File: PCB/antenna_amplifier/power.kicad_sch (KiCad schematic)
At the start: 22 parts, among them J101 PWR_IN 9V, U101 ADM7150ARDZ-5.0, U102 ADM7150ARDZ-3.3

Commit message: Add two-bucket isolated PSU and the PC analysis software
PSU (PCB/acdc_converter/design.py, generated schematic, ERC clean):
Mains -> IRM-05-15 -> LM317 constant-current (0.2 A) / constant-voltage
(10.9 V) supercap charger -> two 4 x 10 F buckets swapped every ~30 s by
two Omron G6K-2 DPDT relays wired in opposite senses. Form-C contacts
break before make, so the receiver ground is never connected to the
charger side; the only coupling left is the open-contact capacitance
(~1 pF) instead of the AC-DC barrier (20-100 pF). The receiver side
adds a reservoir, an LT3045 (0.8 uV rms, EN/PGFB to IN, 22 uF C_SET for
low 1/f noise) and a common-mode choke. Charger ground is bonded to PE
and the enclosure; the only LED is on the mains-powered charger side.

Software (software/elara): streaming decimator, PLL-locked NLMS mains
canceller (>60 dB with drift, 45 Hz tone untouched), L/R Wiener noise
reference subtraction, front-end response correction, Lorentzian
Schumann fit, sferic detector, simulator and CLI; 27 pytest tests.

Generator: explicit wires, net labels on wires, touching and stacked
pins, labels-only symbols.

Co-Authored-By: Claude Opus 5.5 <noreply@anthropic.com>
Claude-Session: https://claude.ai/code/session_01RsM1DhHhY1tSr2aHjVygSC
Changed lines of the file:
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@@
 		(dnp no)
 		(property "Reference" "D102"
-			(at 57.95 61.23 270)
+			(at 57.95 61.23 90)
 			(effects
 				(font
@@
 		)
 		(property "Value" "SMAJ15A"
-			(at 57.95 63.83 270)
+			(at 57.95 63.83 90)
 			(effects
 				(font

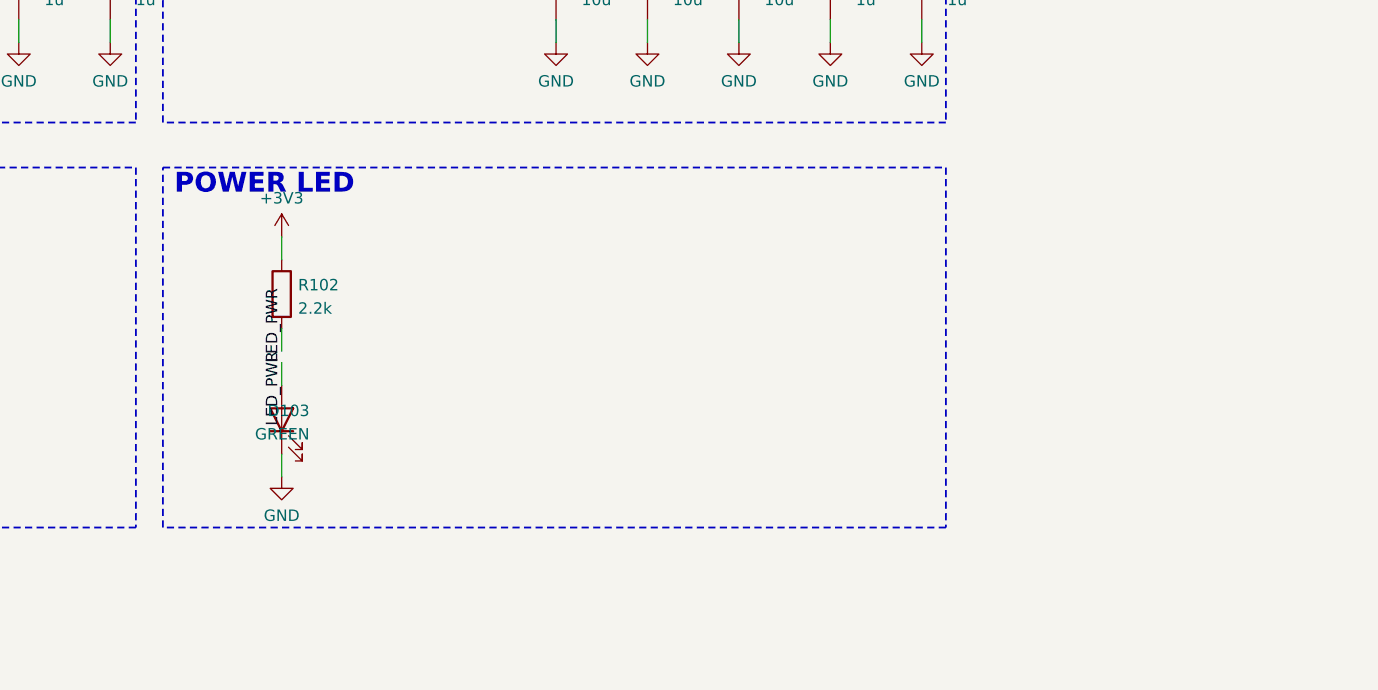
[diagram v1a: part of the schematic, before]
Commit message: Drop amplifier power LED, add turret and pulse-transformer footprints, start PCB generator
The amplifier board can run from a battery, so it has no power LED;
the overload LED only lights while the ADC clips. Adds PCB/elara.pretty
(PTFE input turret, DIP-6 digital-audio transformer outline -- pinout
to be verified against the Newava datasheet) and a work-in-progress
pcbnew-based layout generator.

Co-Authored-By: Claude Opus 5.5 <noreply@anthropic.com>
Claude-Session: https://claude.ai/code/session_01RsM1DhHhY1tSr2aHjVygSC
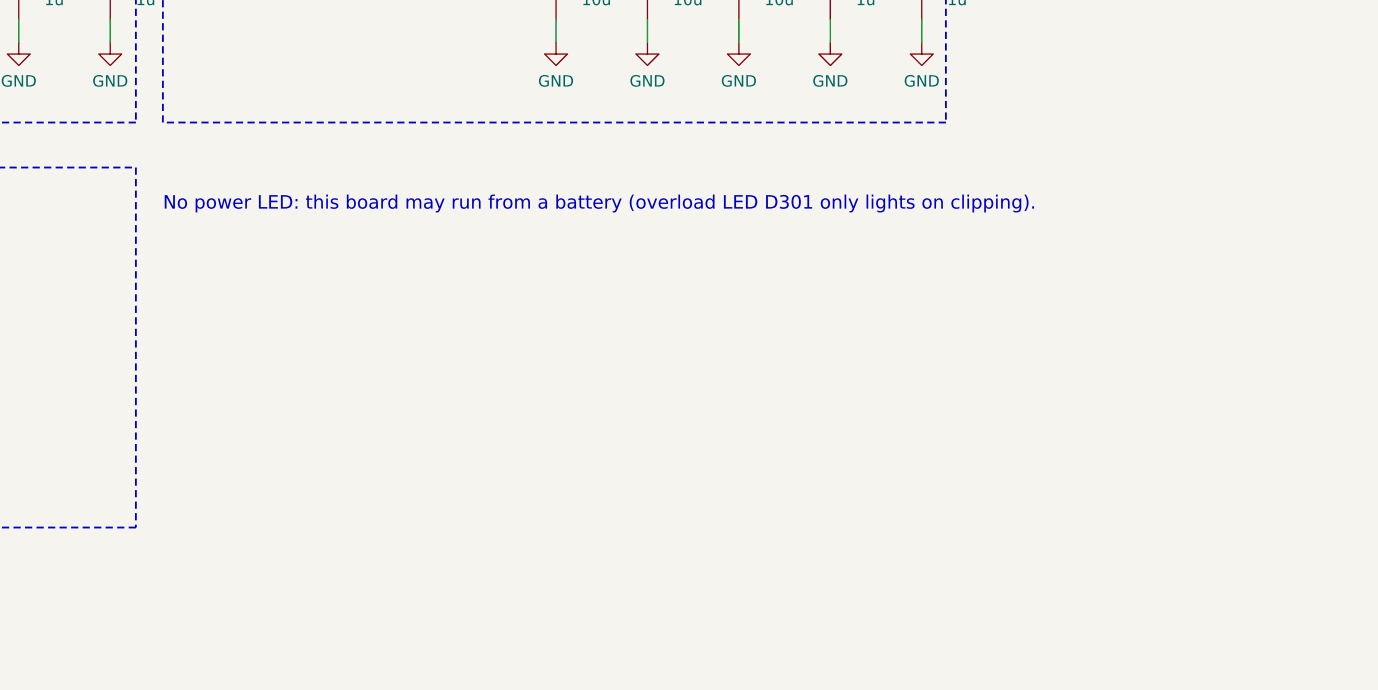
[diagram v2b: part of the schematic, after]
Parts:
- removed D103: GREEN, LED_SMD:LED_0805_2012Metric, symbol Device:LED
- removed R102: 2.2k, Resistor_SMD:R_0603_1608Metric, symbol Device:R
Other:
- note added: "No power LED: this board may run from a battery (overload LED D301 only lights on clipping)."
- note removed: "POWER LED"

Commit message: Route the two-bucket PSU board: fully connected, DRC clean but one thermal
Freerouting 1.9 in batch mode (2.1 never saved its session). Grounds
are routed on this board because the relays switch bucket current in
the unpoured area; mains nets 1.0 mm / 2.0 mm, current paths 0.6 mm;
hand-routed 1 mm PE rail on the left edge, GND_C-PE bond at the PE
hole; only the two mains-side holes are PE, the receiver-side holes
are unplated. Plain exposed-pad footprints (the thermal-via variants
need 0.2 mm drills). Newava S2208x redrawn as a 4-pin part (windings
1-2 / 3-4 per the DCR spec) with slotted pins 2/4 fitting either pitch.

Co-Authored-By: Claude Opus 5.5 <noreply@anthropic.com>
Claude-Session: https://claude.ai/code/session_01RsM1DhHhY1tSr2aHjVygSC
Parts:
- U101, U102: footprint Package_SO:SOIC-8-1EP_3.9x4.9mm_P1.27mm_EP2.29x3mm_ThermalVias -> Package_SO:SOIC-8-1EP_3.9x4.9mm_P1.27mm_EP2.29x3mm
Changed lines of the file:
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@@
 			)
 		)
-		(property "Footprint" "Package_SO:SOIC-8-1EP_3.9x4.9mm_P1.27mm_EP2.29x3mm_ThermalVias"
+		(property "Footprint" "Package_SO:SOIC-8-1EP_3.9x4.9mm_P1.27mm_EP2.29x3mm"
 			(at 123.19 45.72 0)
 			(effects
@@
 			)
 		)
-		(property "Footprint" "Package_SO:SOIC-8-1EP_3.9x4.9mm_P1.27mm_EP2.29x3mm_ThermalVias"
+		(property "Footprint" "Package_SO:SOIC-8-1EP_3.9x4.9mm_P1.27mm_EP2.29x3mm"
 			(at 213.36 45.72 0)
 			(effects

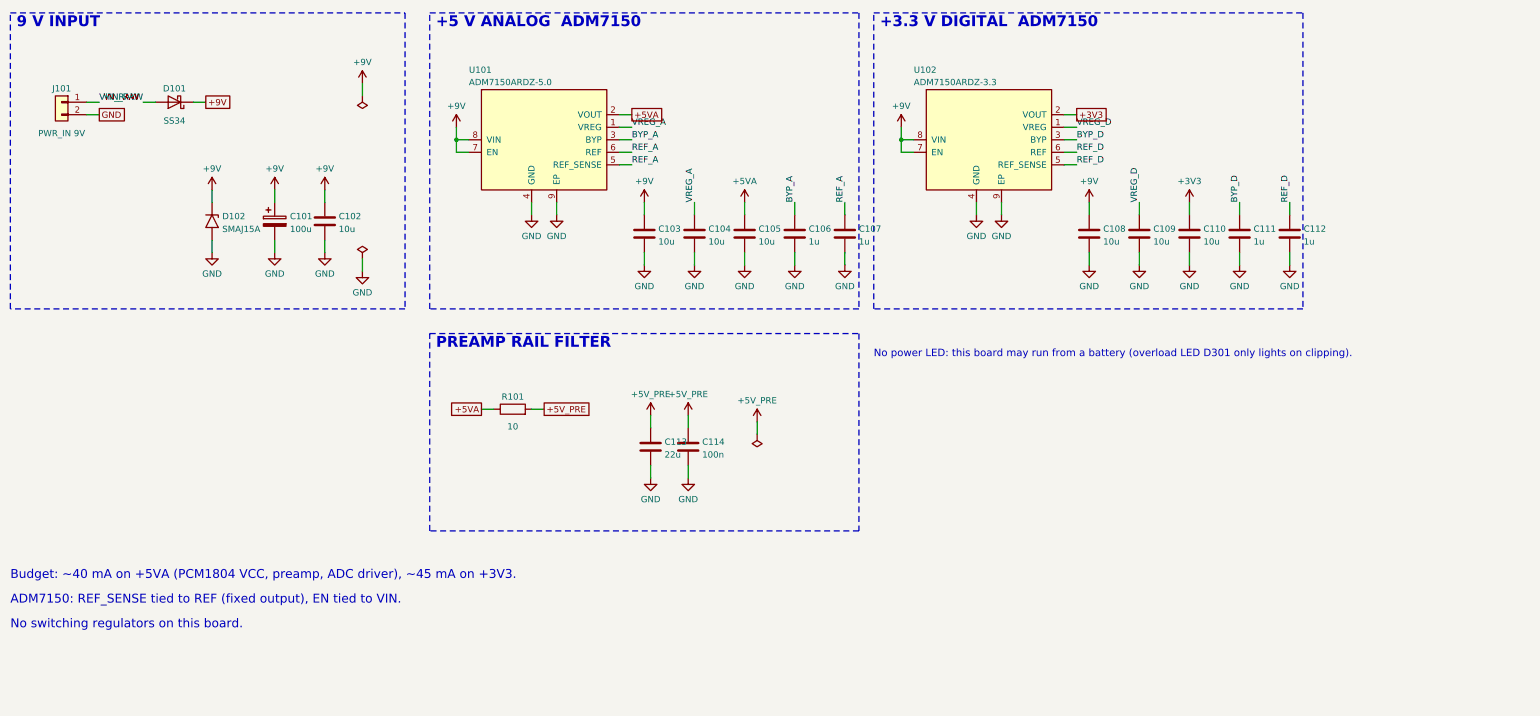
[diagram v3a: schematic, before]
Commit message: Pedantic schematic and silkscreen pass: zero overlaps, labels clear of tracks
Schematics
- tools/kicadgen/schcheck.py checks KiCad's own SVG rendering (exact stroke boxes)
  for text over text, lines through text, crowded twin labels and text outside the
  frame. Both schematics: 0 findings; ERC 0 on both.
- Generator: Sheet.join (one wire + one label instead of two facing labels),
  per-symbol field positions, per-pin stub lengths, shared power symbol for
  adjacent top/bottom rail pins, crowded rail runs get one label, longer PCM1804
  pins (no-connect cross clear of the pin number), PE value clear of its symbol.
- Fixed: doubled VIN_RAW/BIAS_DIV/LED_OVF/CV_ADJ/LED_C labels, +5VA vs VREG,
  +5V_PRE twins, CS8406 GND straps vs neighbours, BNC/LED/diode fields over their
  graphics, bucket-cell values vs tap labels, notes outside the frame, J2 -> J202.
- Root sheet: sub-sheets in signal-flow order with arrows and a design summary;
  dated title blocks.

Boards
- References prefer spots clear of tracks as well as parts (two candidate rings);
  compartment labels are re-placed after routing; the title block on the back is
  placed as one unit; no stitching via under any board text.
- DRC with schematic parity: amplifier 0 errors / 0 unconnected / 0 parity (only
  the intended bare-island mask warnings); PSU and plate 0 of anything.

Co-Authored-By: Claude Opus 5.5 <noreply@anthropic.com>
Claude-Session: https://claude.ai/code/session_01RsM1DhHhY1tSr2aHjVygSC
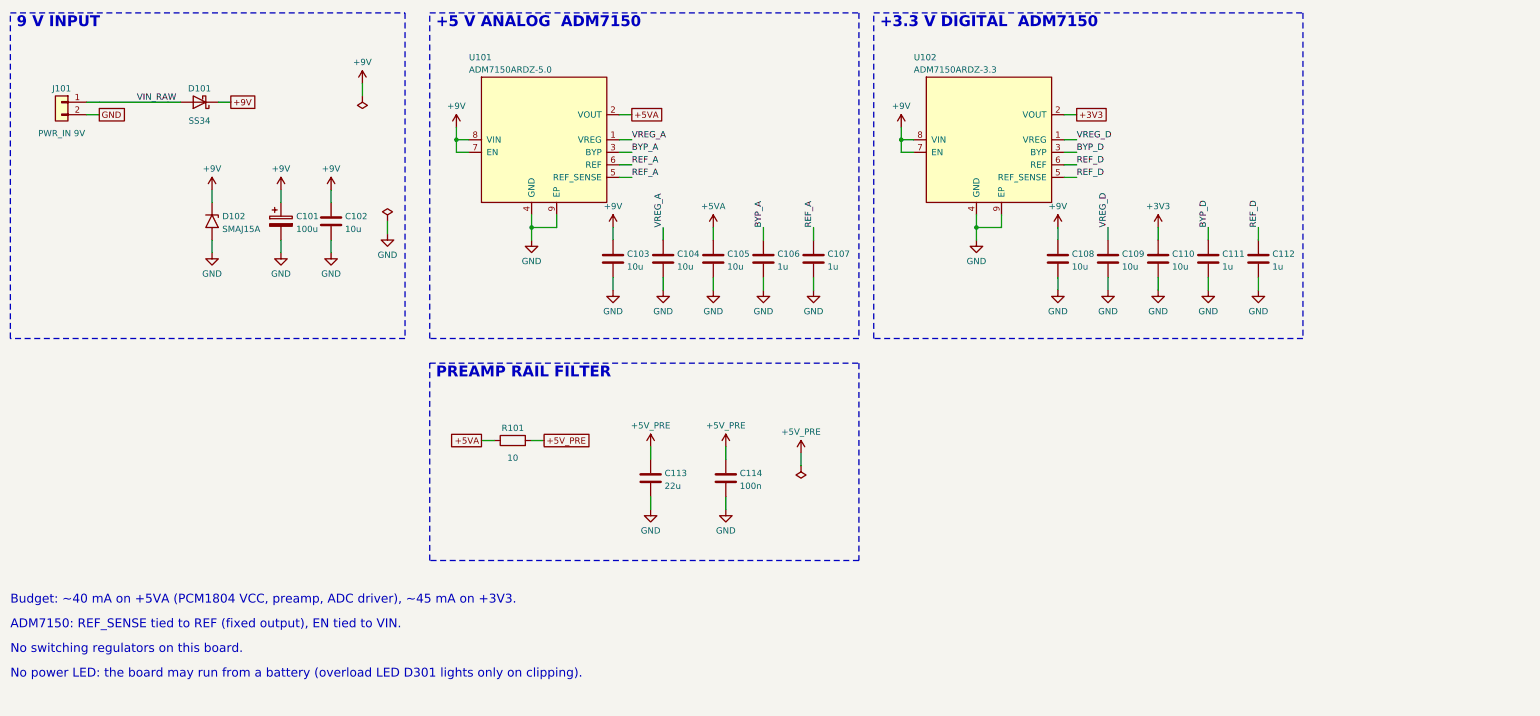
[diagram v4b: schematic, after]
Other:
- note added: "No power LED: the board may run from a battery (overload LED D301 lights only on clipping)."
- note removed: "No power LED: this board may run from a battery (overload LED D301 only lights on clipping)."
- moved on the sheet: C101, C102, C103, C104, C105, C106, C107, C108, C109, C110, C111, C112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

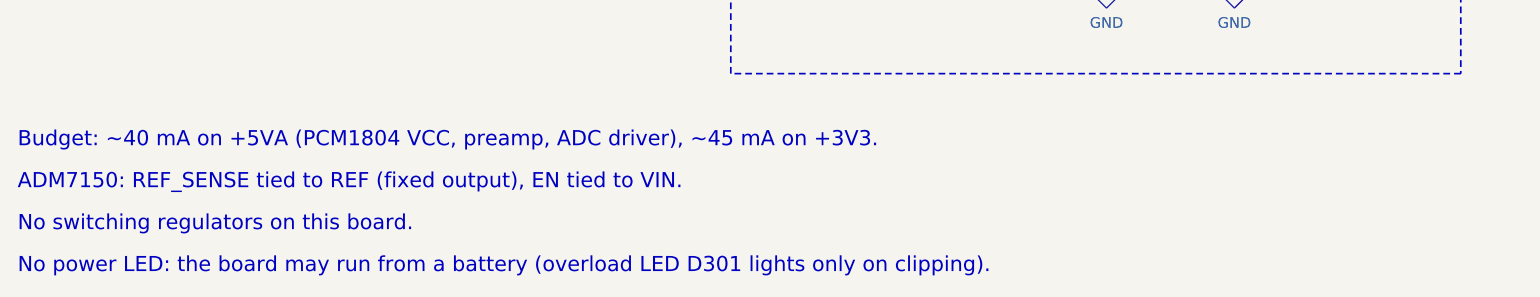
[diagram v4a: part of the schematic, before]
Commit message: Battery-friendly amplifier, RJ45 AES3 output, tidy placement, 1 mm PSU barrier
Amplifier schematic:
- No LEDs (battery use): the D301 overflow LED becomes test point TP301.
- PCM1804 FMT/S-M/OSR pins use the chip's internal 51 k pull-downs (6 resistors
  gone); BYPAS and the CS8406 mode pins get 47 k: about 3 mA less on +3V3.
- One output: AES3 on a shielded RJ45 (Amphenol RJHSE-5380, blue pair 4/5) for
  shielded twisted-pair cable, transformer isolated; the cable shield floats at
  the receiver (10 nF RF bond DNP, the DC bond is gone). The S/PDIF coax branch
  (BNC, second S22083, 5.6 mA standing current) is removed.

Layout:
- Amplifier re-placed in functional blocks on a 0.5 mm grid: PCM1804 and CS8406
  side by side so the I2S lines run straight, capacitor cells round the LDOs,
  DIP pull-downs in line with the switch pins, guard column in signal order with
  a re-routed hand guard-drive link. RJ45 notch 20 x 16 mm, BNC notch gone.
- PSU tidied (aligned columns, flyback diodes over their relays) and the charger
  / receiver copper kept >= 1.0 mm apart (was 0.30 mm): custom DRC rule, 1 mm
  router class for the relay contacts, hand-routed GND / GND_C at the relays.
- Reference labels follow each part's row; every label on silk except on the
  bare guard island. Fixed two placer bugs: each label counted as its own
  obstacle (SWIG proxies compared with 'is'), and unplaced labels blocked their
  neighbours. Texts are measured by their strokes, not KiCad's text cell.

Mechanics: RJ45 notch, plug envelope and a 1 mm isolation gap in fit_check.
BOM: 502 EUR as designed, 407 EUR recommended; 81 order lines.
Docs: STATUS, PLAN, ASSEMBLY, MOUNTING, README, mechanical and BOM notes;
MAINS_CABLE gains a certified DIY screened-cable option (H07RN-F + foil + braid)
and says why Ethernet cable must not carry mains.

All checks pass (tools/check_all.sh): ERC 0, DRC/parity 0 on all boards (only
the intended guard-island mask bridges), mains clearances, fit check, 27 tests.

Co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
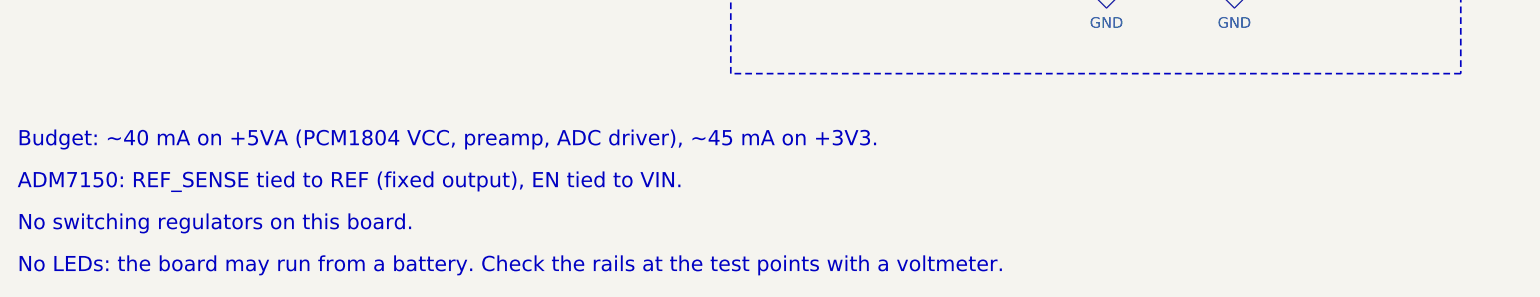
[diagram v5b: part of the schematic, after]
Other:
- note added: "No LEDs: the board may run from a battery. Check the rails at the test points with a voltmeter."
- note removed: "No power LED: the board may run from a battery (overload LED D301 lights only on clipping)."

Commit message: AES3 source resistors 22 ohm for a 111 ohm source; tidy schematics and assembly drawings
- R412/R413 2 x 39 -> 2 x 22 ohm (Vishay TNPW060322R0BEEA, anti-sulfur): the
  CS8406 drivers are 33.5 ohm each at VL = 3.3 V, so 2 x 39 gave a 145 ohm
  source, outside AES3's 110 ohm +-20 %. The schematic note had used the 5 V
  figure and mis-added it.
- AES3 sheet: transformer flipped (kicadgen gains mirror='x') and wired straight
  to R412/R413/C405 and the RJ45, no more touching AES_HOT/AES_COLD labels.
- Stale S/PDIF and 9 V wording out of the sheets and BOM: DC input block reads
  6.98-15 V, J101 'DC IN', PSU J2 'DC OUT', reset button and clock branch say
  AES3; the legacy +9V / +9V_OUT net names are explained on the sheets.
- PSU root sheet gets the same power-path / board summary as the amplifier.
- Assembly drawings: fab-layer copies of the references removed wherever the
  silk reference shows (KiCad 9 texts cannot be hidden), so each part is named
  once; J201/J202 (no silk on the guard island) get theirs beside the part.
- BOM totals +0.14 EUR (502.15 ex VAT reference build, 407.22 recommended).

Co-Authored-By: Claude Opus 5.5 <noreply@anthropic.com>
Claude-Session: https://claude.ai/code/session_01RsM1DhHhY1tSr2aHjVygSC
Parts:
- J101: value PWR_IN 9V -> DC IN
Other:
- note added: "DC INPUT 6.98-15 V"
- note added: "No switching regulators on this board. +9V is the DC bus after D101 (about 6.6 V from the PSU,"
- note added: "up to 15 V from a battery); the net keeps its rev 0.1 name."
- note removed: "9 V INPUT"
- note removed: "No switching regulators on this board."
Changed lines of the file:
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@@
 			)
 		)
-		(property "Value" "PWR_IN 9V"
+		(property "Value" "DC IN"
 			(at 25.4 44.41 0)
 			(effects
@@
 			)
 		)
-		(property "Description" "Micro-Fit 3.0 2-pin right-angle header, 9 V DC in (from PSU or battery)"
+		(property "Description" "Micro-Fit 3.0 2-pin right-angle header, DC in: 6.98 V from the PSU or a 9-15 V battery"
 			(at 25.4 38.1 0)
 			(effects
@@
 		)
 	)
-	(text "9 V INPUT"
+	(text "DC INPUT  6.98-15 V"
 		(exclude_from_sim no)
 		(at 16.27 23.2 0)
@@
 		)
 	)
-	(text "No switching regulators on this board."
+	(text "No switching regulators on this board. +9V is the DC bus after D101 (about 6.6 V from the PSU,"
 		(exclude_from_sim no)
 		(at 15 150 0)
@@
 		)
 	)
-	(text "No LEDs: the board may run from a battery. Check the rails at the test points with a voltmeter."
+	(text "up to 15 V from a battery); the net keeps its rev 0.1 name."
 		(exclude_from_sim no)
 		(at 15 155 0)
 		(effects
 			(font
+				(size 1.8 1.8)
+			)
+			(justify left bottom)
+		)
+	)
+	(text "No LEDs: the board may run from a battery. Check the rails at the test points with a voltmeter."
+		(exclude_from_sim no)
+		(at 15 160 0)
+		(effects
+			(font
